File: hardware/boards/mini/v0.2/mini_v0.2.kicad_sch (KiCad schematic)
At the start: 99 parts, among them IC1 NAU88C22YG, IC3 IS42S16160J-6BLI, J2 Top, J3 Bottom, Q1 PMV37EN22, U1 W25Q128JVP, U2 LTV-217-G, U4 STM32H750XBHx, Y1 Crystal_GND24, Y3 32.768kHz

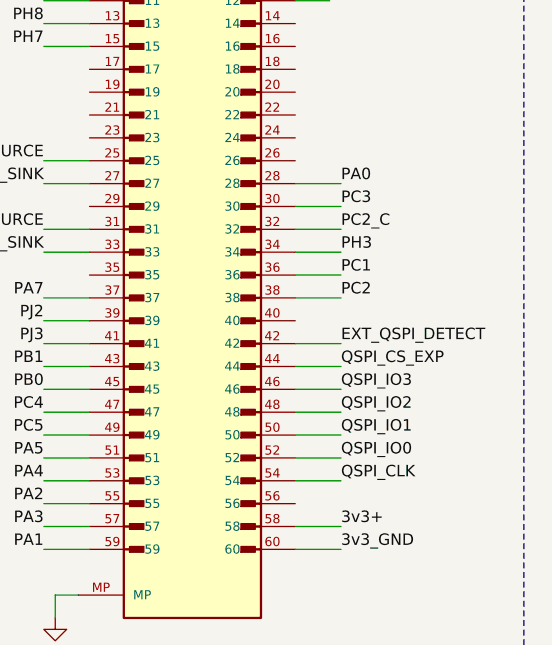
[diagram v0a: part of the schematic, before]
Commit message: mini: various routing cleanup
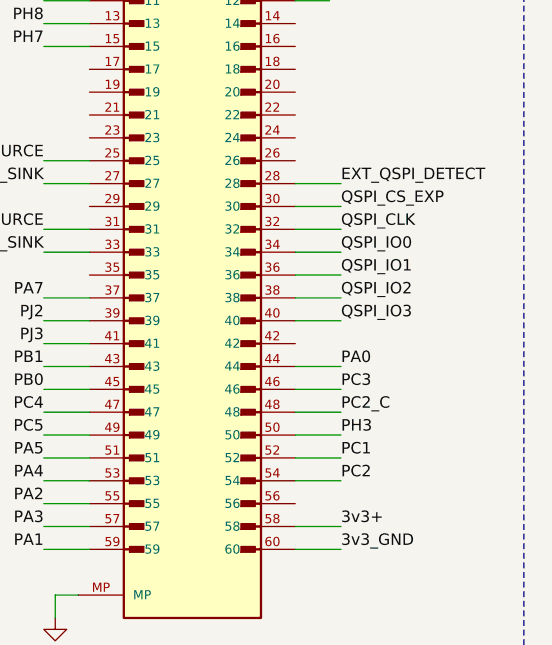
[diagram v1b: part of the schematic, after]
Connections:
- net EXT_QSPI_DETECT: now also J3.28; no longer J3.42
- net PA0: now also J3.44; no longer J3.28
- net PC1: now also J3.52; no longer J3.36
- net PC2: now also J3.54; no longer J3.38
- net PC2_C: now also J3.48; no longer J3.32
- net PC3: now also J3.46; no longer J3.30
- net PH3: now also J3.50; no longer J3.34
- net QSPI_CLK: now also J3.32; no longer J3.54
- net QSPI_CS_EXP: now also J3.30; no longer J3.44
- net QSPI_IO0: now also J3.34; no longer J3.52
- net QSPI_IO1: now also J3.36; no longer J3.50
- net QSPI_IO2: now also J3.38; no longer J3.48
- net QSPI_IO3: now also J3.40; no longer J3.46
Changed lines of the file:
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@@
 	(wire
 		(pts
-			(xy 378.46 215.9) (xy 383.54 215.9)
+			(xy 378.46 198.12) (xy 383.54 198.12)
 		)
 		(stroke
@@
 	(wire
 		(pts
-			(xy 378.46 223.52) (xy 383.54 223.52)
+			(xy 378.46 205.74) (xy 383.54 205.74)
 		)
 		(stroke
@@
 	(wire
 		(pts
-			(xy 378.46 195.58) (xy 383.54 195.58)
+			(xy 378.46 215.9) (xy 383.54 215.9)
 		)
 		(stroke
@@
 	(wire
 		(pts
-			(xy 378.46 210.82) (xy 383.54 210.82)
+			(xy 378.46 193.04) (xy 383.54 193.04)
 		)
 		(stroke
@@
 	(wire
 		(pts
-			(xy 378.46 226.06) (xy 383.54 226.06)
+			(xy 378.46 208.28) (xy 383.54 208.28)
 		)
 		(stroke
@@
 	(wire
 		(pts
-			(xy 378.46 193.04) (xy 383.54 193.04)
+			(xy 378.46 213.36) (xy 383.54 213.36)
 		)
 		(stroke
@@
 	(wire
 		(pts
-			(xy 378.46 205.74) (xy 383.54 205.74)
+			(xy 378.46 226.06) (xy 383.54 226.06)
 		)
 		(stroke
@@
 	(wire
 		(pts
-			(xy 378.46 218.44) (xy 383.54 218.44)
+			(xy 378.46 200.66) (xy 383.54 200.66)
 		)
 		(stroke
@@
 	(wire
 		(pts
-			(xy 378.46 198.12) (xy 383.54 198.12)
+			(xy 378.46 218.44) (xy 383.54 218.44)
 		)
 		(stroke
@@
 	(wire
 		(pts
-			(xy 378.46 200.66) (xy 383.54 200.66)
+			(xy 378.46 220.98) (xy 383.54 220.98)
 		)
 		(stroke
@@
 	(wire
 		(pts
-			(xy 378.46 213.36) (xy 383.54 213.36)
+			(xy 378.46 195.58) (xy 383.54 195.58)
 		)
 		(stroke
@@
 	(wire
 		(pts
-			(xy 378.46 220.98) (xy 383.54 220.98)
+			(xy 378.46 203.2) (xy 383.54 203.2)
 		)
 		(stroke
@@
 	(wire
 		(pts
-			(xy 378.46 203.2) (xy 383.54 203.2)
+			(xy 378.46 223.52) (xy 383.54 223.52)
 		)
 		(stroke
@@
 	)
 	(label "QSPI_IO2"
-		(at 383.54 218.44 0)
+		(at 383.54 205.74 0)
 		(effects
 			(font
@@
 	)
 	(label "PH3"
-		(at 383.54 200.66 0)
+		(at 383.54 220.98 0)
 		(effects
 			(font
@@
 	)
 	(label "QSPI_IO0"
-		(at 383.54 223.52 0)
+		(at 383.54 200.66 0)
 		(effects
 			(font
@@
 	)
 	(label "QSPI_IO1"
-		(at 383.54 220.98 0)
+		(at 383.54 203.2 0)
 		(effects
 			(font
@@
 	)
 	(label "QSPI_CLK"
-		(at 383.54 226.06 0)
+		(at 383.54 198.12 0)
 		(effects
 			(font
@@
 	)
 	(label "PA0"
-		(at 383.54 193.04 0)
+		(at 383.54 213.36 0)
 		(effects
 			(font
@@
 	)
 	(label "PC3"
-		(at 383.54 195.58 0)
+		(at 383.54 215.9 0)
 		(effects
 			(font
@@
 	)
 	(label "PC2"
-		(at 383.54 205.74 0)
+		(at 383.54 226.06 0)
 		(effects
 			(font
@@
 	)
 	(label "EXT_QSPI_DETECT"
-		(at 383.54 210.82 0)
+		(at 383.54 193.04 0)
 		(effects
 			(font
@@
 	)
 	(label "PC2_C"
-		(at 383.54 198.12 0)
+		(at 383.54 218.44 0)
 		(effects
 			(font
@@
 	)
 	(label "QSPI_CS_EXP"
-		(at 383.54 213.36 0)
+		(at 383.54 195.58 0)
 		(effects
 			(font
@@
 	)
 	(label "QSPI_IO3"
-		(at 383.54 215.9 0)
+		(at 383.54 208.28 0)
 		(effects
 			(font
@@
 	)
 	(label "PC1"
-		(at 383.54 203.2 0)
+		(at 383.54 223.52 0)
 		(effects
 			(font

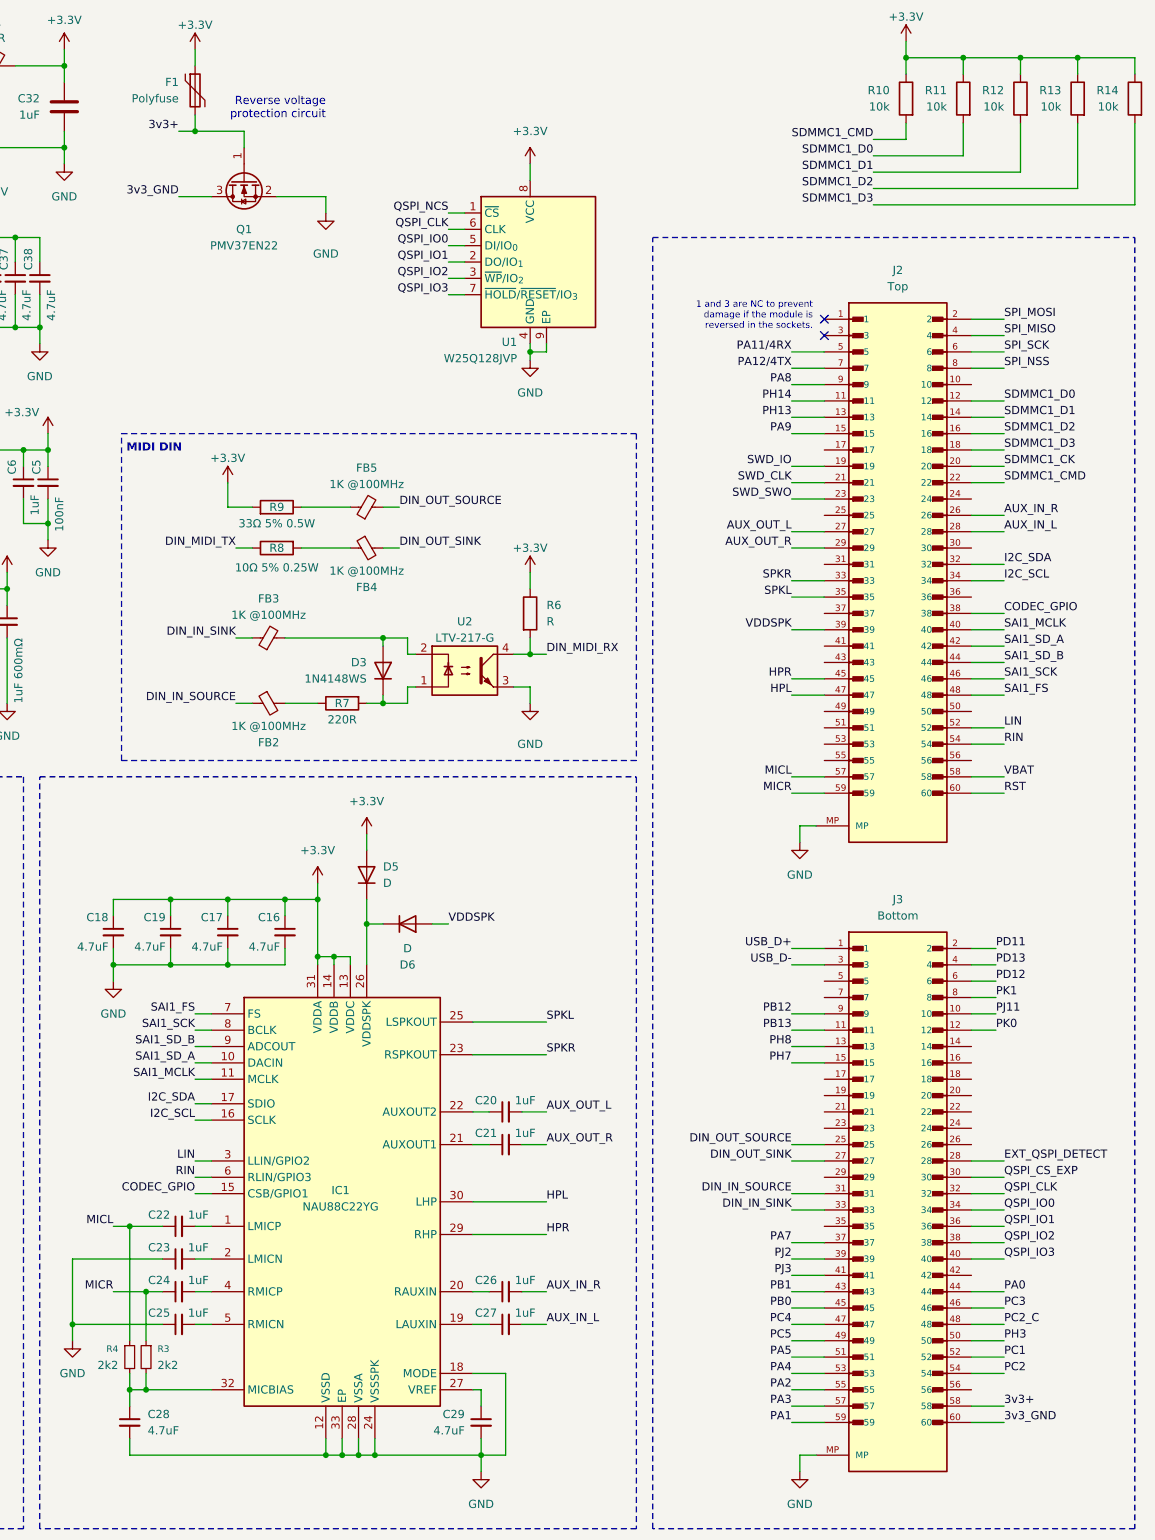
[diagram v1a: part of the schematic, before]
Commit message: mini: route power supply protections
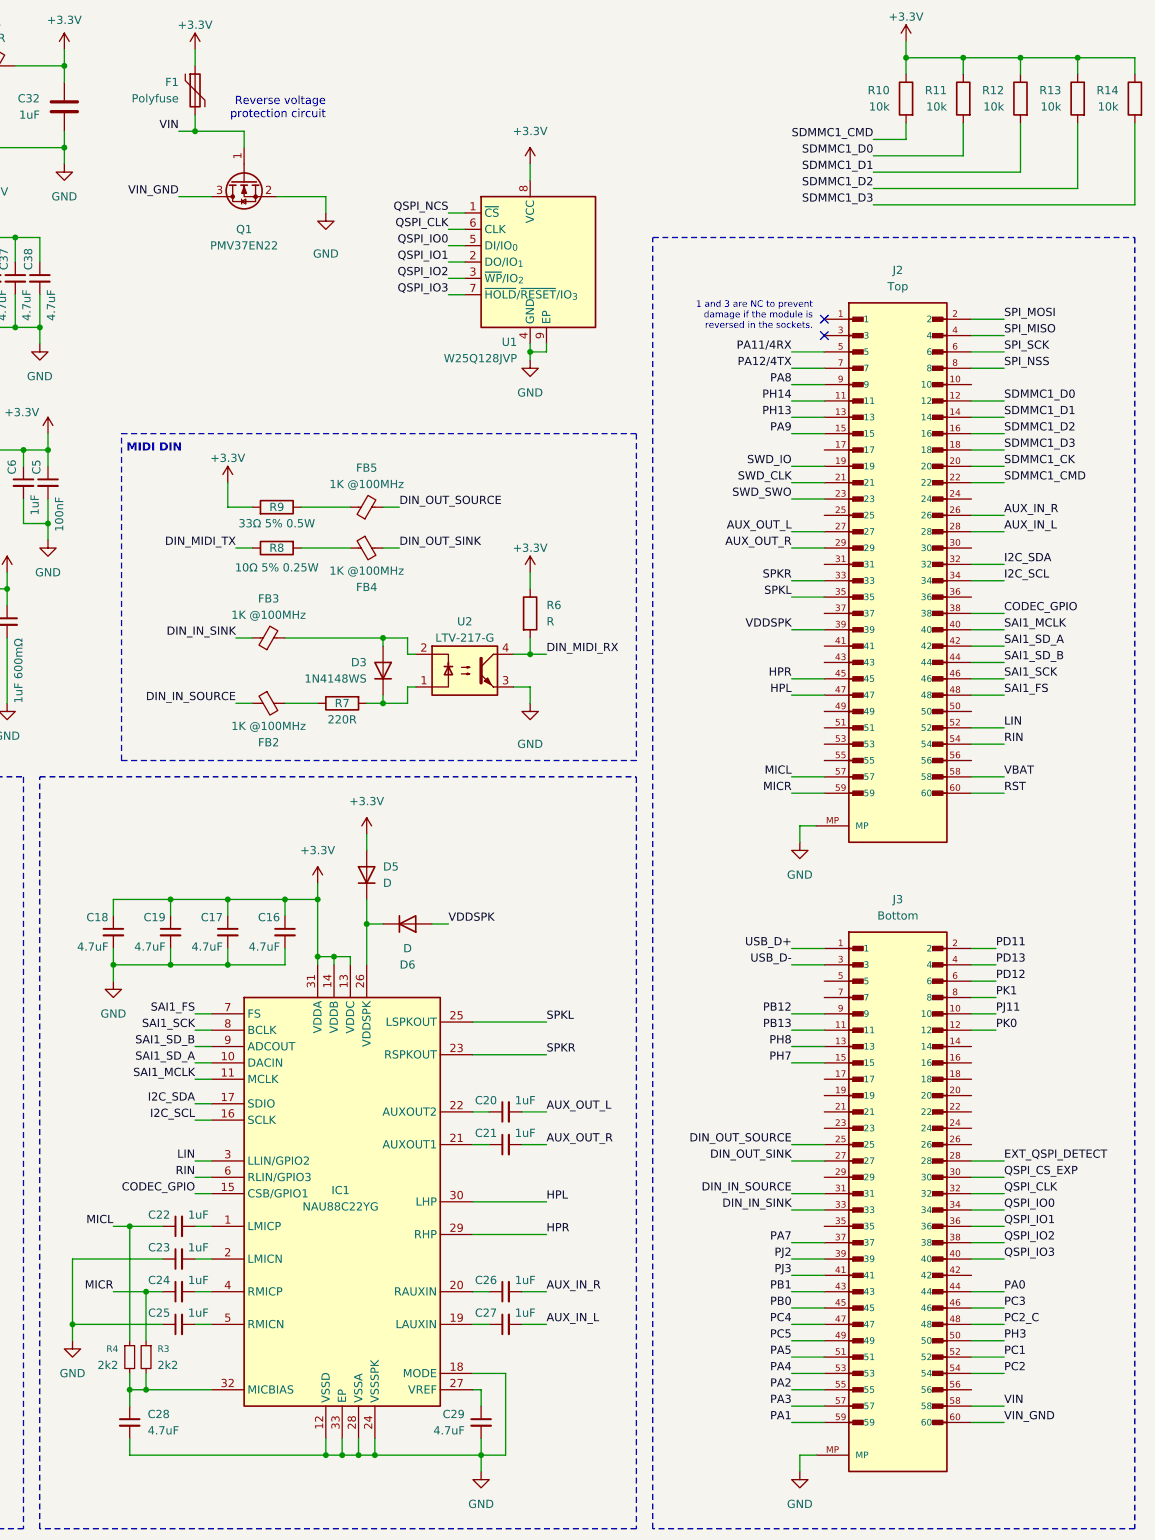
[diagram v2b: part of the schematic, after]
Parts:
- D1: footprint LED_SMD:LED_0603_1608Metric -> LED_SMD:LED_0402_1005Metric
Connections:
- net 3v3+ renamed VIN
- net 3v3_GND renamed VIN_GND
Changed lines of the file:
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@@
 		)
 	)
-	(label "3v3_GND"
+	(label "VIN_GND"
 		(at 383.54 233.68 0)
 		(effects
@@
 		)
 	)
-	(label "3v3+"
+	(label "VIN"
 		(at 255.27 33.02 180)
 		(effects
@@
 		)
 	)
-	(label "3v3+"
+	(label "VIN"
 		(at 383.54 231.14 0)
 		(effects
@@
 		)
 	)
-	(label "3v3_GND"
+	(label "VIN_GND"
 		(at 255.27 43.18 180)
 		(effects
@@
 			)
 		)
-		(property "Footprint" "LED_SMD:LED_0603_1608Metric"
+		(property "Footprint" "LED_SMD:LED_0402_1005Metric"
 			(at 120.65 105.41 0)
 			(effects
